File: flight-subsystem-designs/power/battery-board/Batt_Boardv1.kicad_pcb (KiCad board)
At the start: 2 copper layers, 90.2 x 95.9 mm, 59 parts, among them J1 Conn_02x26_Odd_Even, J2 Conn_02x26_Odd_Even, Q1 IRF7458, Q2 IRF7458, U1 R5460N210AD1, U10 LMV331, U11 TPS7A2601DRVR, U13 74AHC1G32, U14 74AHC1G04, U15 74LVC2G08, U2 BQ29200DRBR, U3 TLA2024IRUGR, U4 LM35-LP, U5 LM35-LP, U6 LM35-LP, U7 LM35-LP, U8 LM4040DBZ-2.5, U9 TMP36xS

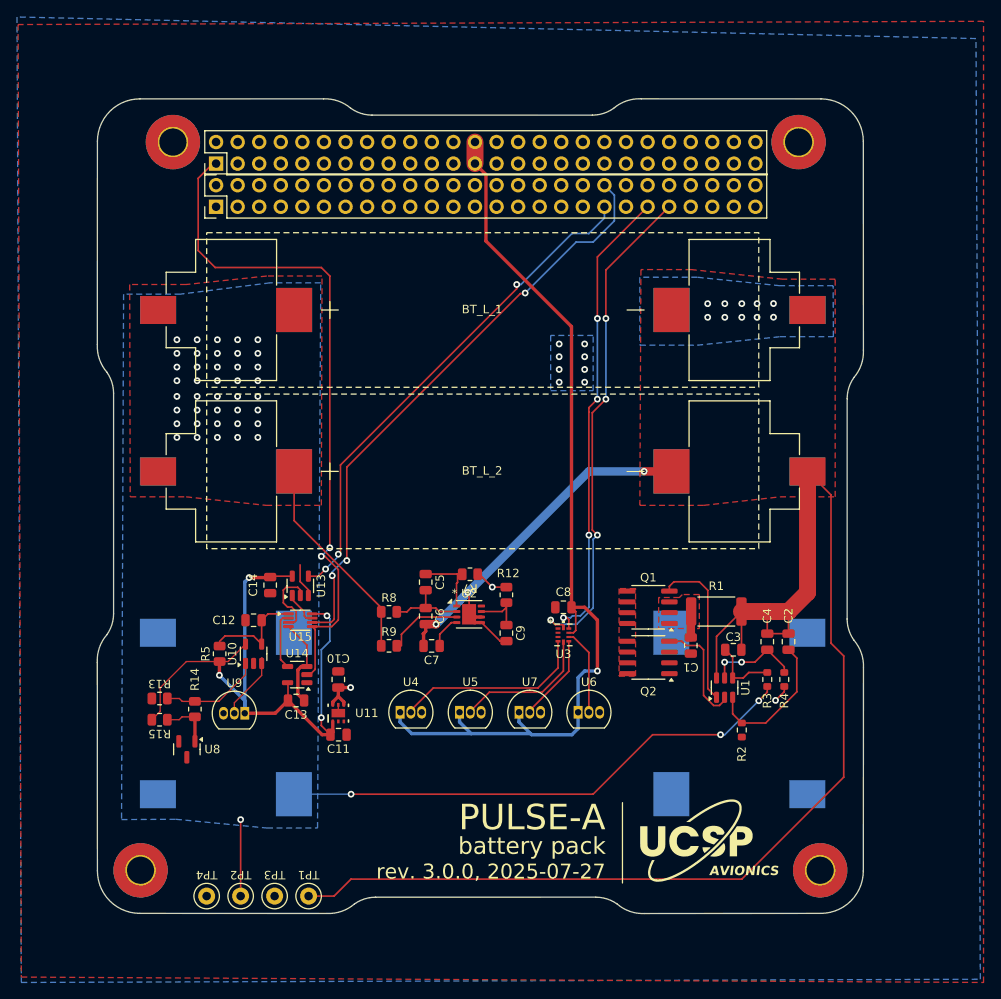
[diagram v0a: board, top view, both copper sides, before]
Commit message: clear up drcs; make pour clearance larger; optimize a bit
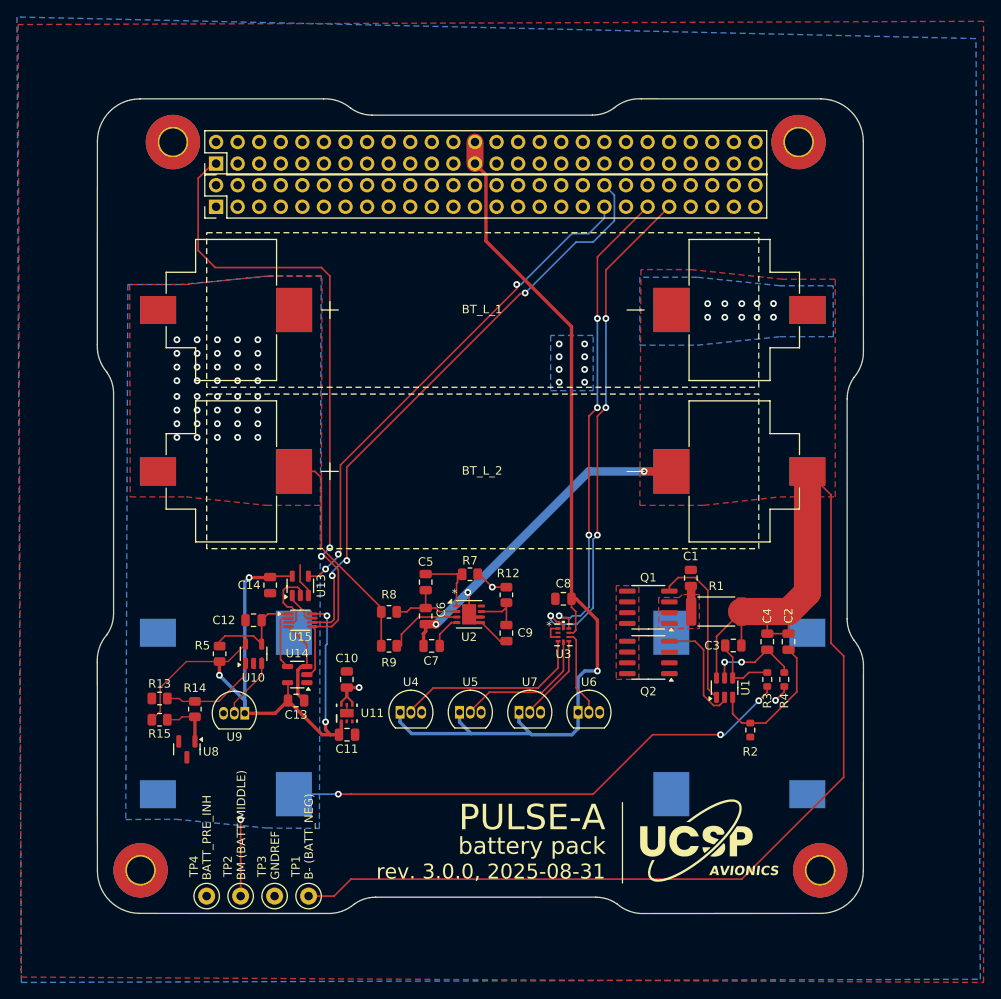
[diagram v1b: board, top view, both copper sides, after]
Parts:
- moved C1 7.95 mm to (169.5, 106.0), turned to 90 degrees
- moved C10 1.00 mm to (129.0, 118.0)
- moved C11 1.00 mm to (129.0, 124.5)
- moved C8 1.00 mm to (154.5, 108.5)
- moved R2 1.00 mm to (176.5, 124.0)
- moved U11 1.00 mm to (129.0, 122.0)
- moved C3 0.50 mm to (174.5, 114.0)
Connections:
- J2 pad 27: +3V3 -> unconnected-(J2-Pin_27-Pad27)
- J2 pad 28: +3V3 -> unconnected-(J2-Pin_28-Pad28)
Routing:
- net GNDREF: track 16.0 -> 18.7 mm
- net /BM: track 95.2 -> 96.6 mm
- net /I2C1_SDA: track 55.3 -> 56.5 mm
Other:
- board text added: "B- (BATT_NEG)"
- board text added: "BATT_PRE_INH"
- board text added: "BM (BATT MIDDLE)"
- board text added: "GNDREF"
- board text added: "rev. 3.0.0, 2025-08-31"
- board text removed: "rev. 3.0.0, 2025-07-27"

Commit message: reroute
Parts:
- added TP5: TestPoint, TestPoint:TestPoint_Loop_D1.80mm_Drill1.0mm_Beaded, F.Cu at (122.5, 143.0)
- moved R15 50.2 mm to (156.2, 113.0), turned to -90 degrees
- moved R5 49.9 mm to (163.5, 108.5), turned to -90 degrees
- moved U14 48.9 mm to (172.1, 116.0)
- moved U13 48.6 mm to (172.1, 108.6)
- moved U15 48.6 mm to (172.1, 112.7)
- moved C14 48.5 mm to (168.5, 107.5), turned to 90 degrees
- moved C12 48.0 mm to (166.0, 108.5), turned to 90 degrees
- moved R13 47.4 mm to (152.6, 107.5)
- moved R14 46.9 mm to (156.2, 108.8)
- moved C13 45.2 mm to (168.1, 117.0), turned to 0 degrees
- moved U8 45.1 mm to (152.6, 111.0)
- moved C2 44.3 mm to (138.0, 124.0), turned to 180 degrees
- moved U10 42.6 mm to (160.2, 108.6), turned to 0 degrees
- moved R2 42.5 mm to (134.0, 122.0), turned to 180 degrees
- moved C10 37.9 mm to (166.5, 113.0), turned to 0 degrees
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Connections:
- J1 pad 36: unconnected-(J1-Pin_36-Pad36) -> KAPTON_SEL
- J2 pad 1: KAPTON_SEL -> unconnected-(J2-Pin_1-Pad1)
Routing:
- net /BM: track 96.6 -> 37.7 mm, vias 44 -> 43
- net /B-: track 198.8 -> 227.1 mm, vias 13 -> 15
- net +5VA: track 78.3 -> 104.0 mm, vias 4 -> 2
- net KAPTON_EN: track 60.1 -> 84.3 mm, vias 3 -> 2
- net KAPTON_OBC_EN: track 69.9 -> 92.4 mm, vias 3 -> 2
- net +5V: track 111.2 -> 132.0 mm, vias 1 -> 4
- net /I2C1_SDA: track 56.5 -> 75.8 mm, vias 4 -> 1
- net /I2C1_SCL: track 59.6 -> 73.3 mm, vias 4 -> 1
- net KAPTON_SEL: track 79.9 -> 93.3 mm
- net Net-(U1-V-): track 16.8 -> 4.19 mm
- net BATT_PRE_INH: track 11.1 -> 19.6 mm
- net Net-(Q1-G): track 19.2 -> 11.0 mm
- net Net-(U10--): track 7.85 -> 15.9 mm
- net Net-(Q2-G): track 13.4 -> 21.3 mm
- net /Heater Control/COMP_REF: track 12.0 -> 5.76 mm
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- removed copper zone on B.Cu, net GNDREF
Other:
- board text added: "5VA (5V ANALOG)"

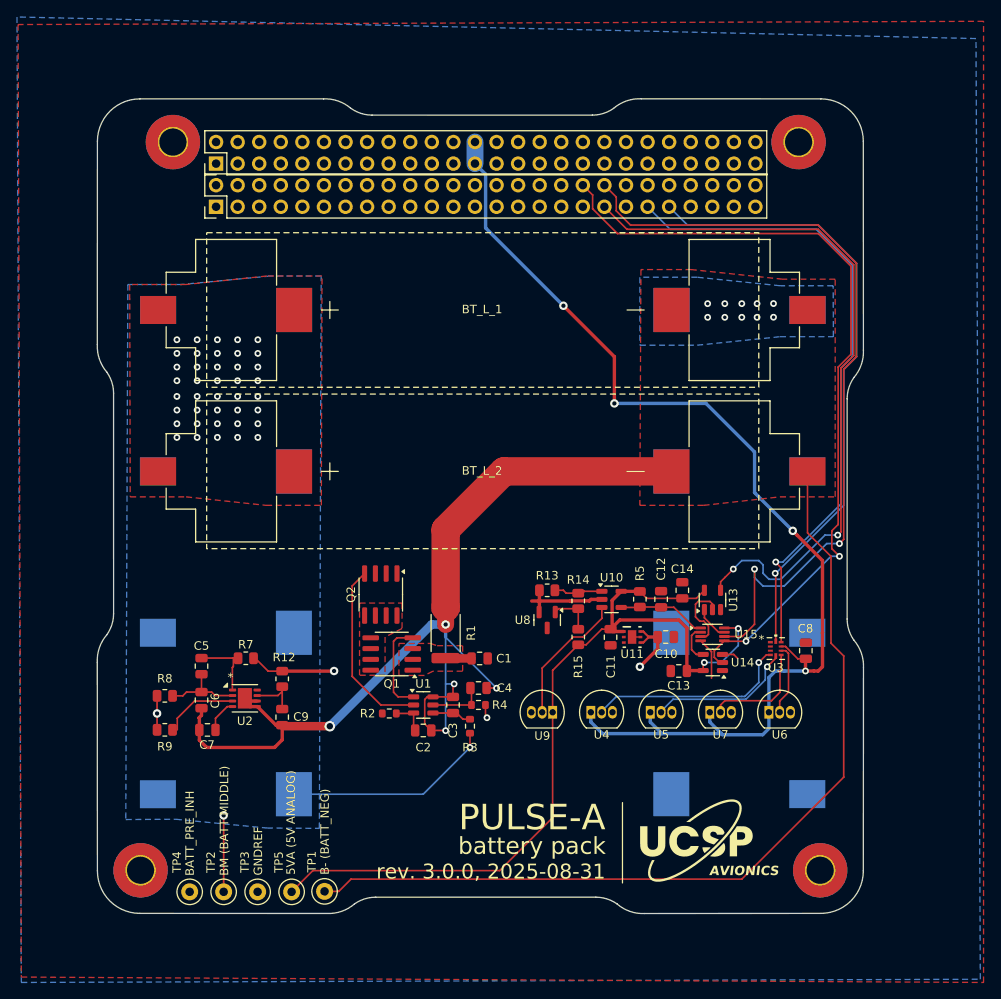
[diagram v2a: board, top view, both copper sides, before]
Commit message: batt_brd: reroute to optimize cu pour currentpaths
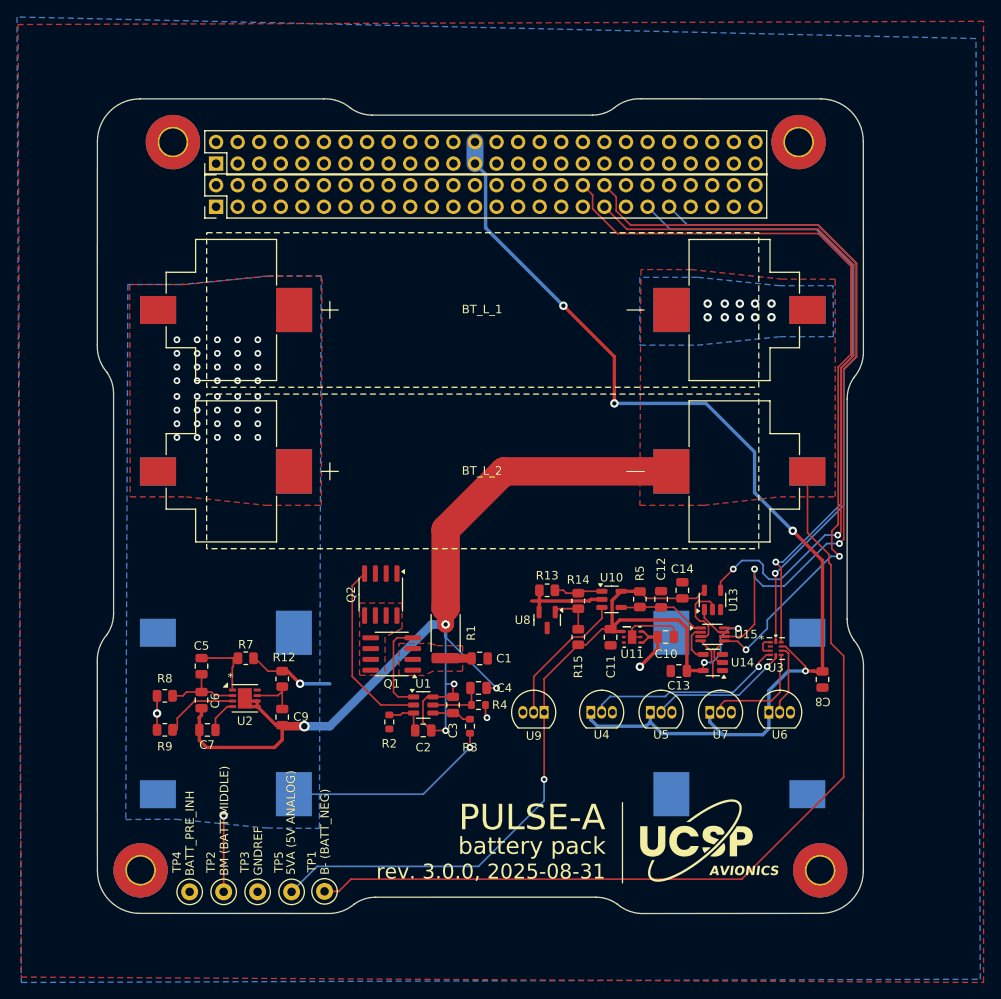
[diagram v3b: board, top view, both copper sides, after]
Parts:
- moved C8 3.92 mm to (185.0, 118.0), turned to -90 degrees
- moved R2 1.00 mm to (134.0, 123.0), turned to -90 degrees
- moved U9 1.00 mm to (149.7, 121.9)
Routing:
- net GNDREF: track 18.8 -> 26.6 mm
- net +5V: track 132.0 -> 129.3 mm
- net +5VA: track 104.0 -> 102.3 mm, vias 2 -> 3
- net KAPTON_SEL: track 93.3 -> 94.7 mm
- net Net-(U1-V-): track 4.19 -> 5.15 mm
- net /B-: track 227.1 -> 227.9 mm
- net Net-(U3-AIN1): track 17.3 -> 16.5 mm
- net Net-(U3-AIN0): track 24.1 -> 23.5 mm
